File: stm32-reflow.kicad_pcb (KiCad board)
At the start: 2 copper layers, 35 parts, among them J1 TC2030, J2 Conn_01x04_Male, J3 Conn_01x03_Male, J4 Screw_Terminal_01x02, J5 Screw_Terminal_01x02, J6 Conn_02x08_Odd_Even, Q1 2N7002, Q10 2N7002, Q11 2N7002, Q2 2N7002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

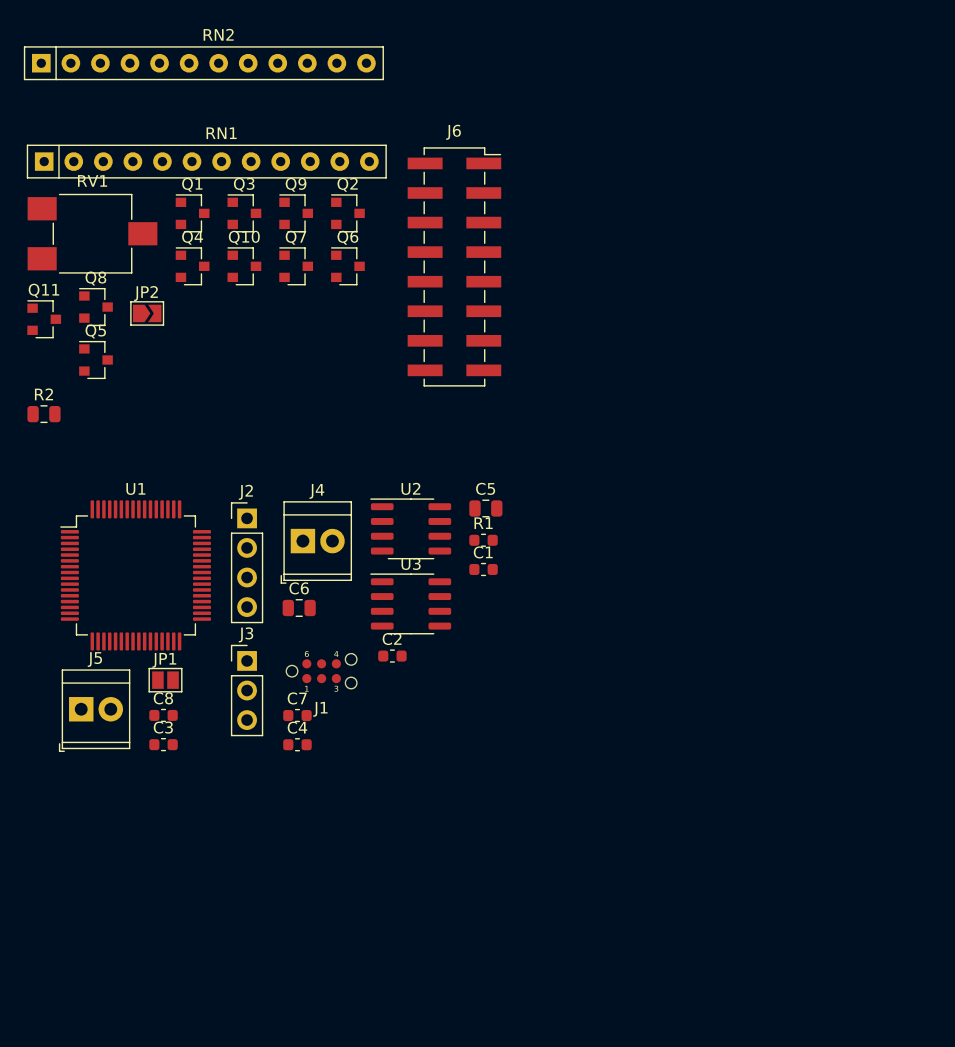
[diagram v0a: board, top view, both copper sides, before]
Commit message: initial routing, added power supply source
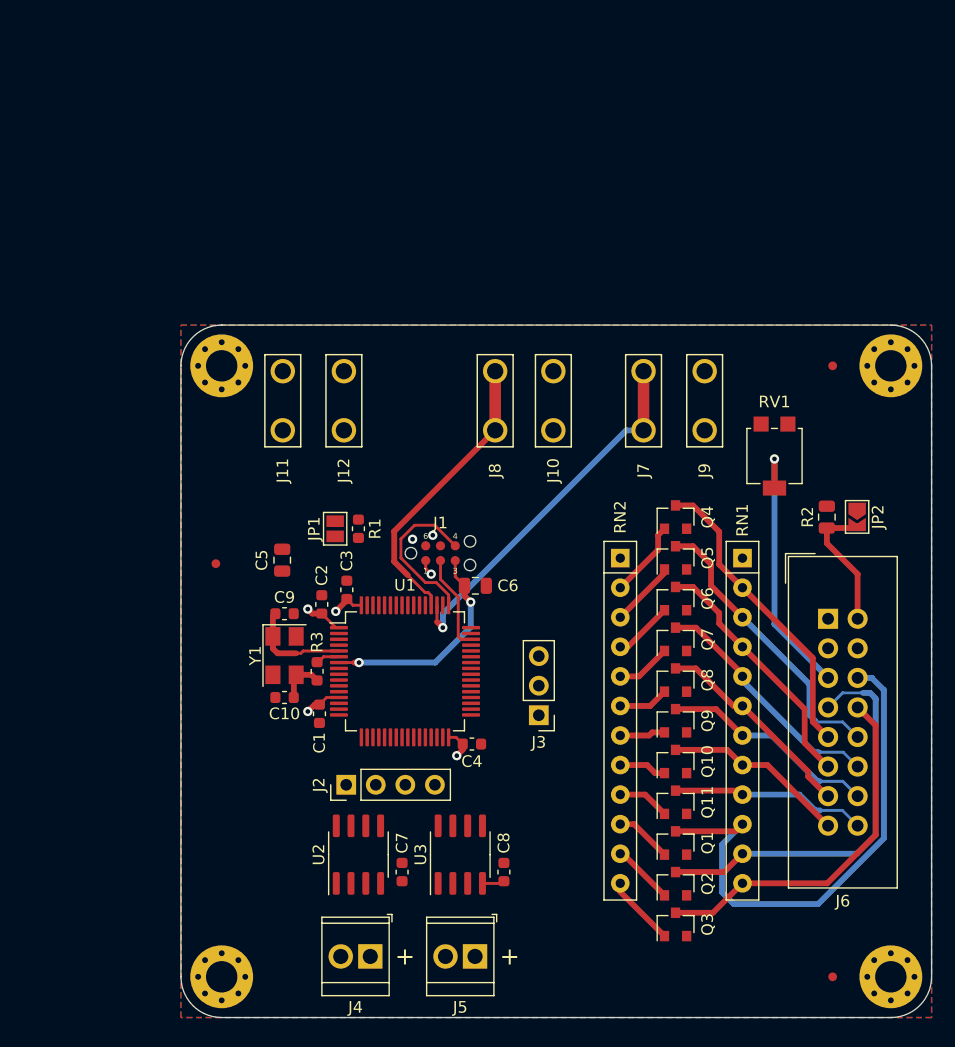
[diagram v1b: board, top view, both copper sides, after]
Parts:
- added C10: 10p, Capacitor_SMD:C_0603_1608Metric, F.Cu at (120.4, 106.0)
- added C9: 10p, Capacitor_SMD:C_0603_1608Metric, F.Cu at (120.4, 98.8)
- added FID1: Fiducial, Fiducial:Fiducial_0.75mm_Mask2.25mm, F.Cu at (167.5, 77.5)
- added FID2: Fiducial, Fiducial:Fiducial_0.75mm_Mask2.25mm, F.Cu at (167.5, 130.0)
- added FID3: Fiducial, Fiducial:Fiducial_0.75mm_Mask2.25mm, F.Cu at (114.5, 94.5)
- added H1: MountingHole, MountingHole:MountingHole_2.7mm_M2.5_Pad_Via, F.Cu at (172.5, 77.5)
- added H2: MountingHole, MountingHole:MountingHole_2.7mm_M2.5_Pad_Via, F.Cu at (115.0, 130.0)
- added H3: MountingHole, MountingHole:MountingHole_2.7mm_M2.5_Pad_Via, F.Cu at (172.5, 130.0)
- added H4: MountingHole, MountingHole:MountingHole_2.7mm_M2.5_Pad_Via, F.Cu at (115.0, 77.5)
- added J10: 63824-1, Personal:CONN_63824-1, F.Cu at (143.5, 80.5)
- added J11: 63824-1, Personal:CONN_63824-1, F.Cu at (120.2, 80.5)
- added J12: 63824-1, Personal:CONN_63824-1, F.Cu at (125.5, 80.5)
- added J7: 63824-1, Personal:CONN_63824-1, F.Cu at (151.2, 80.5)
- added J8: 63824-1, Personal:CONN_63824-1, F.Cu at (138.5, 80.5)
- added J9: 63824-1, Personal:CONN_63824-1, F.Cu at (156.5, 80.5)
- added R3: R_Small, Resistor_SMD:R_0603_1608Metric, F.Cu at (123.2, 103.8)
- added Y1: 8MHz, Crystal:Crystal_SMD_5032-4Pin_5.0x3.2mm, F.Cu at (120.4, 102.4)
- J6: footprint Connector_PinSocket_2.54mm:PinSocket_2x08_P2.54mm_Vertical_SMD -> Connector_IDC:IDC-Header_2x08_P2.54mm_Vertical
- RV1: footprint Potentiometer_SMD:Potentiometer_ACP_CA6-VSMD_Vertical -> Potentiometer_SMD:Potentiometer_Bourns_3314G_Vertical
- moved Q3 71.5 mm to (154.0, 125.5), turned to 90 degrees
- moved RN1 69.0 mm to (159.8, 94.0), turned to -90 degrees
- moved Q11 68.3 mm to (154.0, 115.0), turned to 90 degrees
- moved Q1 68.2 mm to (154.0, 118.5), turned to 90 degrees
- moved R2 67.8 mm to (167.0, 90.5), turned to 90 degrees
- moved RN2 65.4 mm to (149.2, 94.0), turned to -90 degrees
- moved Q2 64.1 mm to (154.0, 122.0), turned to 90 degrees
- moved JP2 63.5 mm to (169.6, 90.5), turned to -90 degrees
- moved RV1 61.6 mm to (162.5, 85.2)
- moved Q8 59.2 mm to (154.0, 104.5), turned to 90 degrees
- moved Q10 56.4 mm to (154.0, 111.5), turned to 90 degrees
- moved Q9 54.4 mm to (154.0, 108.0), turned to 90 degrees
- moved Q5 52.6 mm to (154.0, 94.0), turned to 90 degrees
- moved Q4 46.8 mm to (154.0, 90.5), turned to 90 degrees
- moved Q7 45.7 mm to (154.0, 101.0), turned to 90 degrees
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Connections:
- J1 pad 3: /Reflow MCU/NRST -> /Reflow MCU/~{NRST}
- RN2 pad 10: /Reflow Level Shifting/DB5 -> /Reflow Level Shifting/RS
- RN2 pad 11: /Reflow Level Shifting/DB6 -> /Reflow Level Shifting/R/~{W}
- RN2 pad 12: /Reflow Level Shifting/DB7 -> /Reflow Level Shifting/E
- RN2 pad 2: /Reflow Level Shifting/E -> /Reflow Level Shifting/DB0
- RN2 pad 3: /Reflow Level Shifting/R/~{W} -> /Reflow Level Shifting/DB1
- RN2 pad 4: /Reflow Level Shifting/RS -> /Reflow Level Shifting/DB2
- RN2 pad 5: /Reflow Level Shifting/DB0 -> /Reflow Level Shifting/DB3
- RN2 pad 6: /Reflow Level Shifting/DB1 -> /Reflow Level Shifting/DB4
- RN2 pad 7: /Reflow Level Shifting/DB2 -> /Reflow Level Shifting/DB5
- RN2 pad 8: /Reflow Level Shifting/DB3 -> /Reflow Level Shifting/DB6
- RN2 pad 9: /Reflow Level Shifting/DB4 -> /Reflow Level Shifting/DB7
- U1 pad 51: unconnected-(U1-Pad51) -> /Reflow MCU/R1E
- U1 pad 52: unconnected-(U1-Pad52) -> /Reflow MCU/R2E
- U1 pad 7: /Reflow MCU/NRST -> /Reflow MCU/~{NRST}
- U3 pad 4: unconnected-(U3-Pad4) -> +3V3
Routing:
- net /Reflow Level Shifting/LRS: track 0.00 -> 44.7 mm
- net /Reflow Level Shifting/LR/~{W}: track 0.00 -> 35.0 mm
- net /Reflow MCU/R1E: track 0.00 -> 32.2 mm, vias 0 -> 1
- net /Reflow Level Shifting/LE: track 0.00 -> 31.6 mm
- net /Reflow Level Shifting/LDB0: track 0.00 -> 26.2 mm
- net /Reflow MCU/R2E: track 0.00 -> 25.2 mm
- net /Reflow Level Shifting/LDB1: track 0.00 -> 25.1 mm
- net /Reflow Level Shifting/VEE: track 0.00 -> 23.2 mm, vias 0 -> 1
- net /Reflow Level Shifting/LDB2: track 0.00 -> 21.7 mm
- net /Reflow Level Shifting/LDB3: track 0.00 -> 20.9 mm
- net /Reflow MCU/~{NRST}: track 0.00 -> 18.9 mm, vias 0 -> 2
- net /Reflow Level Shifting/LDB5: track 0.00 -> 18.7 mm
- net /Reflow Level Shifting/LDB4: track 0.00 -> 17.9 mm
- net /Reflow Level Shifting/LDB7: track 0.00 -> 16.9 mm
- net /Reflow Level Shifting/LDB6: track 0.00 -> 15.8 mm
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- added copper zone on In2.Cu, net +3V3
- added copper zone on In2.Cu, net +5V
- added copper zone on B.Cu, net GND
- added copper zone on F.Cu, net GND
- added copper zone on In1.Cu, net GND
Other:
- board outline added: 64.5 x 59.5 mm
- copper layers 2 -> 4
- board text added: "+"

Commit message: finalized routing and circuit schematic (so far)
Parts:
- added G***: LOGO, Personal:db_logo_10mm, F.Cu at (117.6, 115.4)
- added G***: LOGO, Personal:db_logo, B.Cu at (122.8, 91.6)
- added Q12: 2N7002, Package_TO_SOT_SMD:SOT-23, F.Cu at (162.0, 80.5)
- added Q13: 2N7002, Package_TO_SOT_SMD:SOT-23, F.Cu at (148.0, 86.0)
- added R4: 10k, Resistor_SMD:R_0603_1608Metric, F.Cu at (164.5, 80.5)
- added R5: 10k, Resistor_SMD:R_0603_1608Metric, F.Cu at (148.0, 88.5)
- added REF**: OSHW-Symbol_8.9x8mm_SilkScreen, Symbol:OSHW-Symbol_8.9x8mm_SilkScreen, F.Cu at (161.4, 128.2)
- added U4: LM1117-3.3, Package_TO_SOT_SMD:SOT-223-3_TabPin2, F.Cu at (132.0, 80.8)
- moved C5 9.37 mm to (128.0, 89.0), turned to 180 degrees
- moved FID3 5.55 mm to (120.0, 93.8)
- moved RV1 5.51 mm to (168.0, 85.5), turned to -90 degrees
- moved FID2 3.76 mm to (167.2, 126.2)
- moved FID1 2.85 mm to (164.8, 76.8)
- moved JP1 0.75 mm to (124.0, 91.5)
- moved R1 0.75 mm to (126.0, 91.5), turned to 90 degrees
- moved H1 0.56 mm to (172.0, 77.8)
- moved H3 0.56 mm to (172.0, 129.8)
- moved J10 0.50 mm to (144.0, 80.5)
- moved J9 0.50 mm to (157.0, 80.5)
- moved H2 0.25 mm to (115.0, 129.8)
- moved H4 0.25 mm to (115.0, 77.8)
- moved J7 0.25 mm to (151.5, 80.5)
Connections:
- J10 pad 1: GND -> Net-(J10-Pad1)
- J10 pad 2: GND -> Net-(J10-Pad1)
- J7 pad 1: /Reflow MCU/R1E -> +5V
- J7 pad 2: /Reflow MCU/R1E -> +5V
- J8 pad 1: /Reflow MCU/R2E -> +5V
- J8 pad 2: /Reflow MCU/R2E -> +5V
- J9 pad 1: GND -> Net-(J9-Pad1)
- J9 pad 2: GND -> Net-(J9-Pad1)
- U3 pad 6: /Reflow MCU/CS0 -> /Reflow MCU/CS1
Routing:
- net /Reflow Level Shifting/R/~{W}: track 5.28 -> 57.0 mm, vias 0 -> 2
- net /Reflow Level Shifting/E: track 6.11 -> 52.4 mm, vias 0 -> 1
- net /Reflow Level Shifting/DB0: track 6.64 -> 39.9 mm, vias 0 -> 1
- net /Reflow Level Shifting/DB1: track 5.68 -> 36.3 mm, vias 0 -> 1
- net +5V: track 0.00 -> 30.5 mm, vias 0 -> 1
- net /Reflow MCU/SCK: track 0.00 -> 29.7 mm
- net /Reflow Level Shifting/DB7: track 4.49 -> 33.9 mm, vias 0 -> 1
- net /Reflow Level Shifting/DB2: track 5.10 -> 34.3 mm, vias 0 -> 1
- net /Reflow Level Shifting/DB6: track 4.09 -> 31.7 mm, vias 0 -> 1
- net /Reflow MCU/CS0: track 0.00 -> 26.8 mm, vias 0 -> 2
- net /Reflow Level Shifting/DB5: track 3.91 -> 30.6 mm, vias 0 -> 1
- net /Reflow Level Shifting/DB4: track 4.31 -> 30.7 mm, vias 0 -> 1
- net /Reflow Level Shifting/DB3: track 4.71 -> 30.7 mm, vias 0 -> 1
- net /Reflow Level Shifting/RS: track 4.88 -> 24.7 mm
- net /Reflow MCU/MISO: track 0.00 -> 17.7 mm
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- added copper zone on F.Cu, net +3V3
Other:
- board size 64.5 x 59.5 mm -> 64 x 59 mm
- board text added: "Copyright (c) 2021 Bastian de Byl"
- board text added: "STM32 Reflow Board"
- board text added: "STM32 Reflow Board Designed by Bastian de Byl"

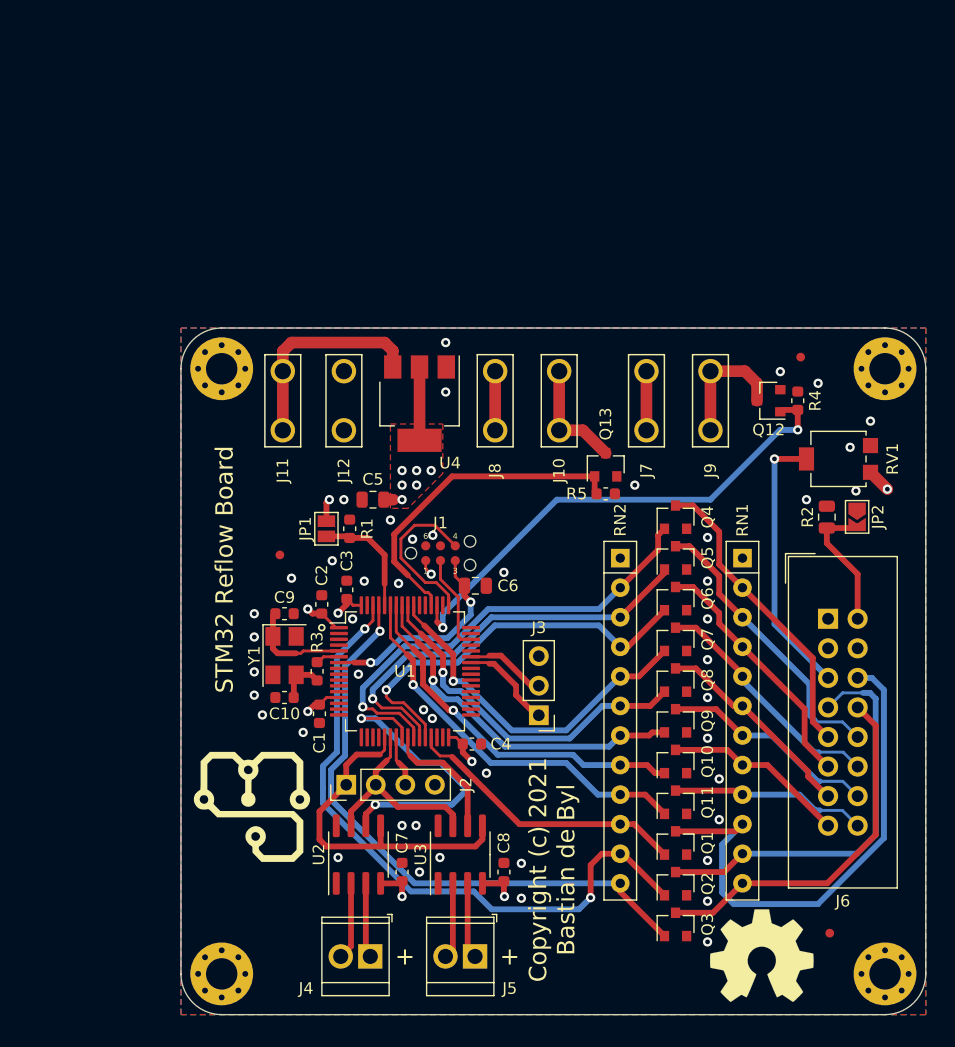
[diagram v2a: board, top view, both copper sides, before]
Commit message: fixed orientation of the LCD IDC connector
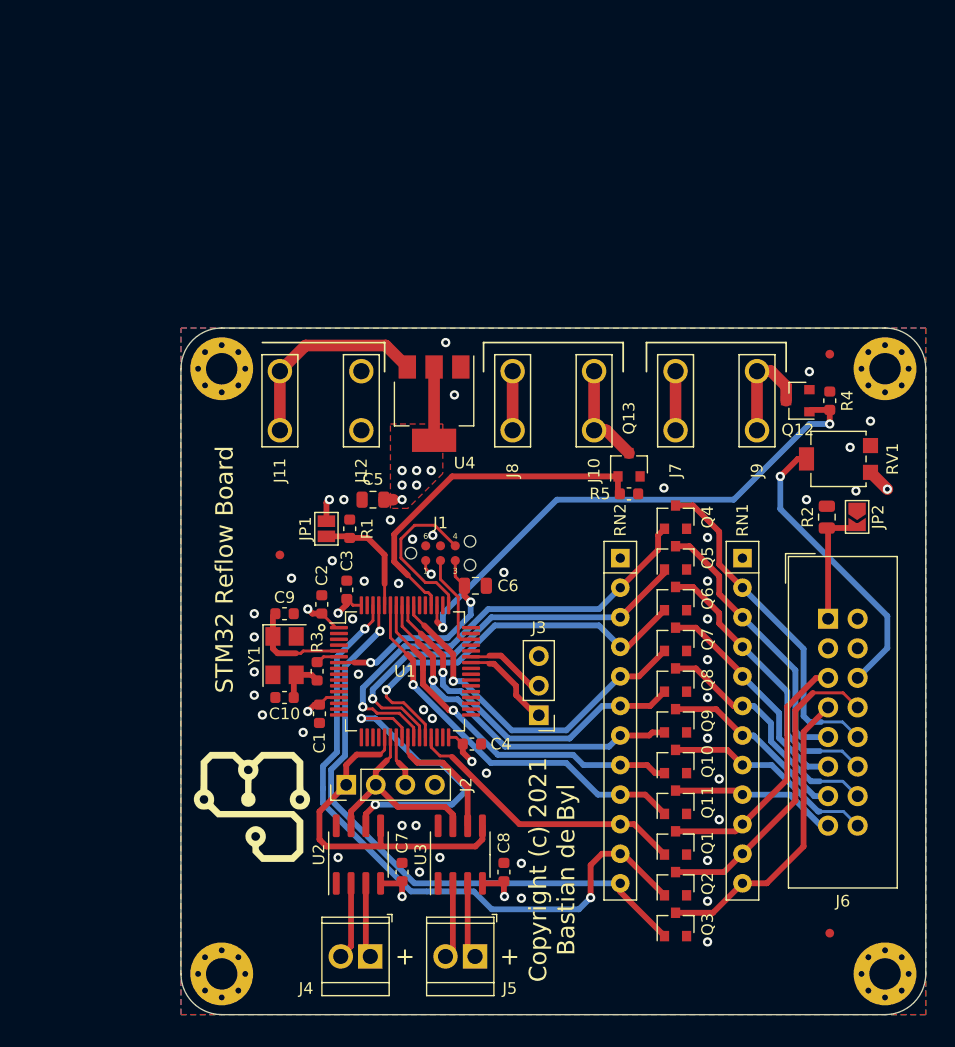
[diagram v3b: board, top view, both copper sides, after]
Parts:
- removed REF**: OSHW-Symbol_8.9x8mm_SilkScreen, Symbol:OSHW-Symbol_8.9x8mm_SilkScreen
- moved J9 4.00 mm to (161.0, 80.5)
- moved J10 3.00 mm to (147.0, 80.5)
- moved R4 2.75 mm to (167.2, 80.5)
- moved FID1 2.51 mm to (167.2, 76.5)
- moved J7 2.50 mm to (154.0, 80.5)
- moved Q12 2.50 mm to (164.5, 80.5)
- moved Q13 2.00 mm to (150.0, 86.0)
- moved R5 2.00 mm to (150.0, 88.5)
- moved J12 1.50 mm to (127.0, 80.5)
- moved J8 1.50 mm to (140.0, 80.5)
- moved U4 1.25 mm to (133.2, 80.8)
- moved J11 0.25 mm to (120.0, 80.5)
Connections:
- J6 pad 1: +5V -> /Reflow Level Shifting/LEDK
- J6 pad 10: /Reflow Level Shifting/LDB1 -> /Reflow Level Shifting/LDB0
- J6 pad 11: /Reflow Level Shifting/LDB2 -> /Reflow Level Shifting/LDB3
- J6 pad 12: /Reflow Level Shifting/LDB3 -> /Reflow Level Shifting/LDB2
- J6 pad 13: /Reflow Level Shifting/LDB4 -> /Reflow Level Shifting/LDB5
- J6 pad 14: /Reflow Level Shifting/LDB5 -> /Reflow Level Shifting/LDB4
- J6 pad 15: /Reflow Level Shifting/LDB6 -> /Reflow Level Shifting/LDB7
- J6 pad 16: /Reflow Level Shifting/LDB7 -> /Reflow Level Shifting/LDB6
- J6 pad 2: /Reflow Level Shifting/LEDK -> +5V
- J6 pad 3: GND -> +5V
- J6 pad 4: +5V -> GND
- J6 pad 5: /Reflow Level Shifting/VEE -> /Reflow Level Shifting/LRS
- J6 pad 6: /Reflow Level Shifting/LRS -> /Reflow Level Shifting/VEE
- J6 pad 7: /Reflow Level Shifting/LR/~{W} -> /Reflow Level Shifting/LE
- J6 pad 8: /Reflow Level Shifting/LE -> /Reflow Level Shifting/LR/~{W}
- J6 pad 9: /Reflow Level Shifting/LDB0 -> /Reflow Level Shifting/LDB1
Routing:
- net /Reflow Level Shifting/LRS: track 44.7 -> 22.2 mm
- net /Reflow Level Shifting/LR/~{W}: track 35.0 -> 27.1 mm
- net /Reflow Level Shifting/LE: track 31.6 -> 26.2 mm
- net /Reflow Level Shifting/LDB4: track 17.9 -> 21.1 mm
- net /Reflow Level Shifting/LDB2: track 21.7 -> 24.7 mm
- net /Reflow Level Shifting/LDB0: track 26.2 -> 28.9 mm
- net /Reflow MCU/R1E: track 43.7 -> 46.4 mm
- net /Reflow Level Shifting/LDB5: track 18.7 -> 16.2 mm
- net /Reflow Level Shifting/LDB7: track 16.9 -> 14.4 mm
- net /Reflow Level Shifting/LDB6: track 15.8 -> 18.3 mm
- net /Reflow MCU/R2E: track 28.4 -> 30.4 mm
- net Net-(J9-Pad1): track 11.0 -> 9.36 mm
- net /Reflow Level Shifting/VEE: track 23.5 -> 25.1 mm
- net /Reflow Level Shifting/LDB3: track 20.9 -> 19.4 mm
- net /Reflow Level Shifting/LEDK: track 11.3 -> 10.1 mm
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
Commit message: ERC and DRC fixes
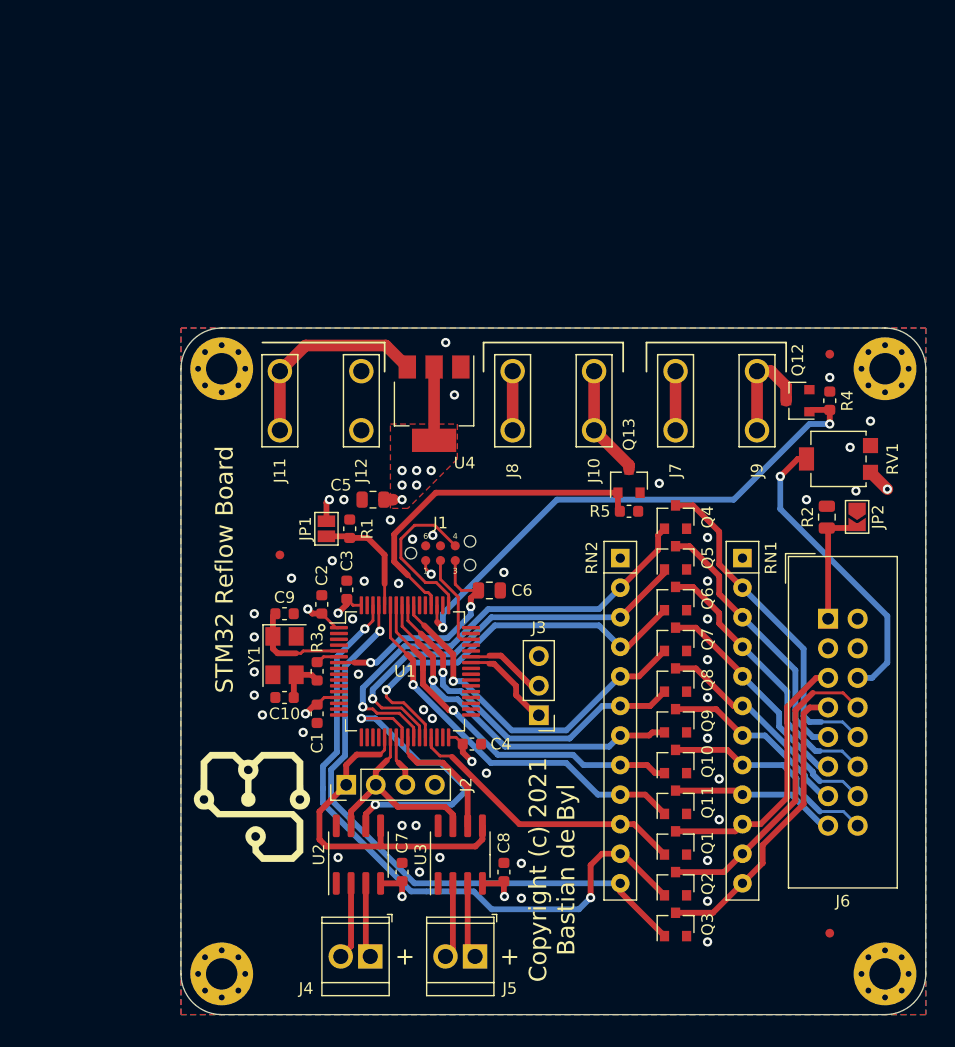
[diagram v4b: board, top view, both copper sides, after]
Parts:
- moved R5 1.50 mm to (150.0, 90.0)
- moved Q13 1.40 mm to (150.0, 87.4)
- moved C6 1.26 mm to (138.0, 96.8)
- moved C1 0.20 mm to (123.2, 107.4)
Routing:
- net /Reflow MCU/~{NRST}: track 18.2 -> 19.6 mm
- net /Reflow Level Shifting/LRS: track 22.2 -> 23.1 mm
- net /Reflow Level Shifting/LDB4: track 21.1 -> 20.3 mm
- net Net-(J10-Pad2): track 8.89 -> 9.68 mm
- net /Reflow Level Shifting/VEE: track 25.1 -> 25.8 mm
- net /Reflow Level Shifting/LDB1: track 23.9 -> 23.3 mm
- net /Reflow Level Shifting/LDB2: track 24.7 -> 24.1 mm
- net /Reflow Level Shifting/LDB3: track 19.4 -> 18.8 mm
- net /Reflow Level Shifting/LE: track 26.2 -> 25.7 mm
